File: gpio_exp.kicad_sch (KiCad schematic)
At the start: 11 parts, among them U11 MCP23S17_SO

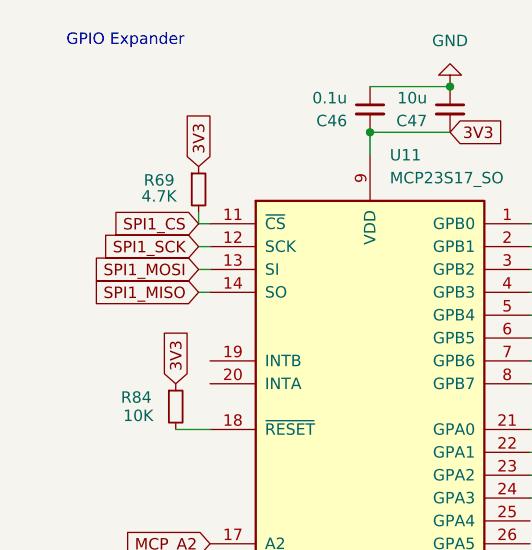
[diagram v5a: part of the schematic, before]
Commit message: yerleştirme tamamlandı
3d modeller eklenecek
drc kontrolü yapılacak
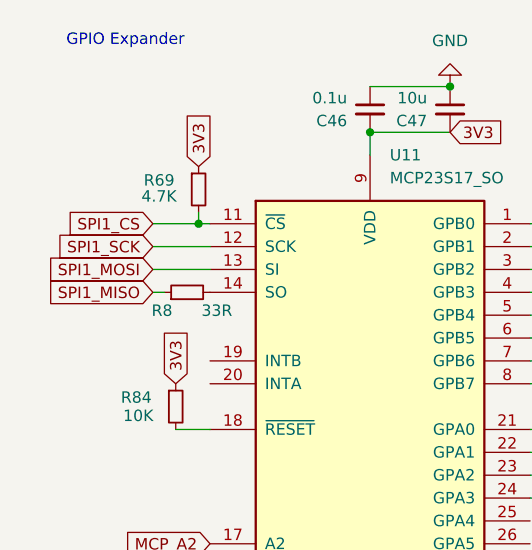
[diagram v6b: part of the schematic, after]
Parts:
- added R8: 33R, Resistor_SMD:R_0805_2012Metric, symbol Device:R_Small
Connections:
- net SPI1_MISO: now also R8.1; no longer U11.14 (SO)
- new net: R8.2, U11.14 (SO)
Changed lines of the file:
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@@
+	)
+	(junction
+		(at 31.75 35.56)
+		(diameter 0)
+		(color 0 0 0 0)
 	)
 	(junction
@@
 	(wire
 		(pts
+			(xy 26.67 35.56) (xy 31.75 35.56)
+		)
+		(stroke
+			(width 0)
+			(type default)
+		)
+	)
+	(wire
+		(pts
 			(xy 118.11 39.37) (xy 118.11 49.53)
 		)
@@
 	(wire
 		(pts
-			(xy 31.75 43.18) (xy 33.02 43.18)
-		)
-		(stroke
-			(width 0)
-			(type default)
-		)
-	)
-	(wire
-		(pts
 			(xy 71.12 38.1) (xy 68.58 38.1)
 		)
@@
 	(wire
 		(pts
+			(xy 71.12 60.96) (xy 68.58 60.96)
+		)
+		(stroke
+			(width 0)
+			(type default)
+		)
+	)
+	(wire
+		(pts
+			(xy 71.12 58.42) (xy 68.58 58.42)
+		)
+		(stroke
+			(width 0)
+			(type default)
+		)
+	)
+	(wire
+		(pts
+			(xy 26.67 40.64) (xy 33.02 40.64)
+		)
+		(stroke
+			(width 0)
+			(type default)
+		)
+	)
+	(polyline
+		(pts
+			(xy 12.7 90.17) (xy 151.13 90.17)
+		)
+		(stroke
+			(width 0)
+			(type default)
+		)
+	)
+	(wire
+		(pts
 			(xy 31.75 35.56) (xy 33.02 35.56)
 		)
@@
 	(wire
 		(pts
-			(xy 71.12 60.96) (xy 68.58 60.96)
-		)
-		(stroke
-			(width 0)
-			(type default)
-		)
-	)
-	(wire
-		(pts
-			(xy 71.12 58.42) (xy 68.58 58.42)
-		)
-		(stroke
-			(width 0)
-			(type default)
-		)
-	)
-	(wire
-		(pts
-			(xy 31.75 40.64) (xy 33.02 40.64)
+			(xy 125.73 29.21) (xy 130.81 29.21)
+		)
+		(stroke
+			(width 0)
+			(type default)
+		)
+	)
+	(wire
+		(pts
+			(xy 71.12 63.5) (xy 68.58 63.5)
+		)
+		(stroke
+			(width 0)
+			(type default)
+		)
+	)
+	(wire
+		(pts
+			(xy 31.75 35.56) (xy 31.75 34.29)
+		)
+		(stroke
+			(width 0)
+			(type default)
+		)
+	)
+	(wire
+		(pts
+			(xy 26.67 38.1) (xy 33.02 38.1)
+		)
+		(stroke
+			(width 0)
+			(type default)
+		)
+	)
+	(wire
+		(pts
+			(xy 135.89 39.37) (xy 135.89 49.53)
+		)
+		(stroke
+			(width 0)
+			(type default)
+		)
+	)
+	(wire
+		(pts
+			(xy 50.8 25.4) (xy 50.8 27.94)
+		)
+		(stroke
+			(width 0)
+			(type default)
+		)
+	)
+	(wire
+		(pts
+			(xy 26.67 43.18) (xy 27.94 43.18)
+		)
+		(stroke
+			(width 0)
+			(type default)
+		)
+	)
+	(wire
+		(pts
+			(xy 68.58 45.72) (xy 71.12 45.72)
 		)
 		(stroke
@@
 	(polyline
 		(pts
-			(xy 12.7 90.17) (xy 151.13 90.17)
-		)
-		(stroke
-			(width 0)
-			(type default)
-		)
-	)
-	(wire
-		(pts
-			(xy 125.73 29.21) (xy 130.81 29.21)
-		)
-		(stroke
-			(width 0)
-			(type default)
-		)
-	)
-	(wire
-		(pts
-			(xy 71.12 63.5) (xy 68.58 63.5)
-		)
-		(stroke
-			(width 0)
-			(type default)
-		)
-	)
-	(wire
-		(pts
-			(xy 31.75 38.1) (xy 33.02 38.1)
-		)
-		(stroke
-			(width 0)
-			(type default)
-		)
-	)
-	(wire
-		(pts
-			(xy 135.89 39.37) (xy 135.89 49.53)
-		)
-		(stroke
-			(width 0)
-			(type default)
-		)
-	)
-	(wire
-		(pts
-			(xy 50.8 25.4) (xy 50.8 27.94)
-		)
-		(stroke
-			(width 0)
-			(type default)
-		)
-	)
-	(wire
-		(pts
-			(xy 68.58 45.72) (xy 71.12 45.72)
-		)
-		(stroke
-			(width 0)
-			(type default)
-		)
-	)
-	(polyline
-		(pts
 			(xy 106.68 12.7) (xy 106.68 90.17)
-		)
-		(stroke
-			(width 0)
-			(type default)
-		)
-	)
-	(wire
-		(pts
-			(xy 31.75 34.29) (xy 31.75 35.56)
 		)
 		(stroke
@@
 	(global_label "SPI1_SCK"
 		(shape input)
-		(at 31.75 38.1 180)
+		(at 26.67 38.1 180)
 		(fields_autoplaced yes)
 		(effects
@@
 		)
 		(property "Intersheetrefs" "${INTERSHEET_REFS}"
-			(at 19.7539 38.1 0)
+			(at 14.6739 38.1 0)
 			(effects
 				(font
@@
 	(global_label "SPI1_MISO"
 		(shape input)
-		(at 31.75 43.18 180)
+		(at 26.67 43.18 180)
 		(fields_autoplaced yes)
 		(effects
@@
 		)
 		(property "Intersheetrefs" "${INTERSHEET_REFS}"
-			(at 18.9072 43.18 0)
+			(at 13.8272 43.18 0)
 			(effects
 				(font
@@
 	(global_label "SPI1_MOSI"
 		(shape input)
-		(at 31.75 40.64 180)
+		(at 26.67 40.64 180)
 		(fields_autoplaced yes)
 		(effects
@@
 		)
 		(property "Intersheetrefs" "${INTERSHEET_REFS}"
-			(at 18.9072 40.64 0)
+			(at 13.8272 40.64 0)
 			(effects
 				(font
@@
 	(global_label "SPI1_CS"
 		(shape input)
-		(at 31.75 35.56 180)
+		(at 26.67 35.56 180)
 		(fields_autoplaced yes)
 		(effects
@@
 		)
 		(property "Intersheetrefs" "${INTERSHEET_REFS}"
-			(at 21.0239 35.56 0)
+			(at 15.9439 35.56 0)
 			(effects
 				(font
@@
 					(unit 1)
 				)
+			)
+		)
+	)
+	(symbol
+		(lib_id "Device:R_Small")
+		(at 30.48 43.18 90)
+		(unit 1)
+		(exclude_from_sim no)
+		(in_bom yes)
+		(on_board yes)
+		(dnp no)
+		(property "Reference" "R8"
+			(at 27.686 45.212 90)
+			(effects
+				(font
+					(size 1.27 1.27)
+				)
+			)
+		)
+		(property "Value" "33R"
+			(at 33.782 45.212 90)
+			(effects
+				(font
+					(size 1.27 1.27)
+				)
+			)
+		)
+		(property "Footprint" "Resistor_SMD:R_0805_2012Metric"
+			(at 30.48 43.18 0)
+			(effects
+				(font
+					(size 1.27 1.27)
+				)
+				(hide yes)
+			)
+		)
+		(property "Datasheet" "~"
+			(at 30.48 43.18 0)
+			(effects
+				(font
+					(size 1.27 1.27)
+				)
+				(hide yes)
+			)
+		)
+		(property "Description" "Resistor, small symbol"
+			(at 30.48 43.18 0)
+			(effects
+				(font
+					(size 1.27 1.27)
+				)
+				(hide yes)
+			)
+		)
+		(pin "1"
+		)
+		(pin "2"
+		)
+		(instances
+			(project "controllerForVehicle"
+				(path "/f177fb06-71dc-4865-9331-a828b12c2bf7/cf99d41f-154f-4525-9df8-a364b4903864"
+					(reference "R8")
+					(unit 1)
+				)
